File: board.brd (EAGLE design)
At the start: 92.1 x 90.5 mm, 64 parts, among them K1 FTR-K1C, K2 FTR-K1C, K3 FTR-K1C, K4 FTR-K1C, X6 PN61729-S

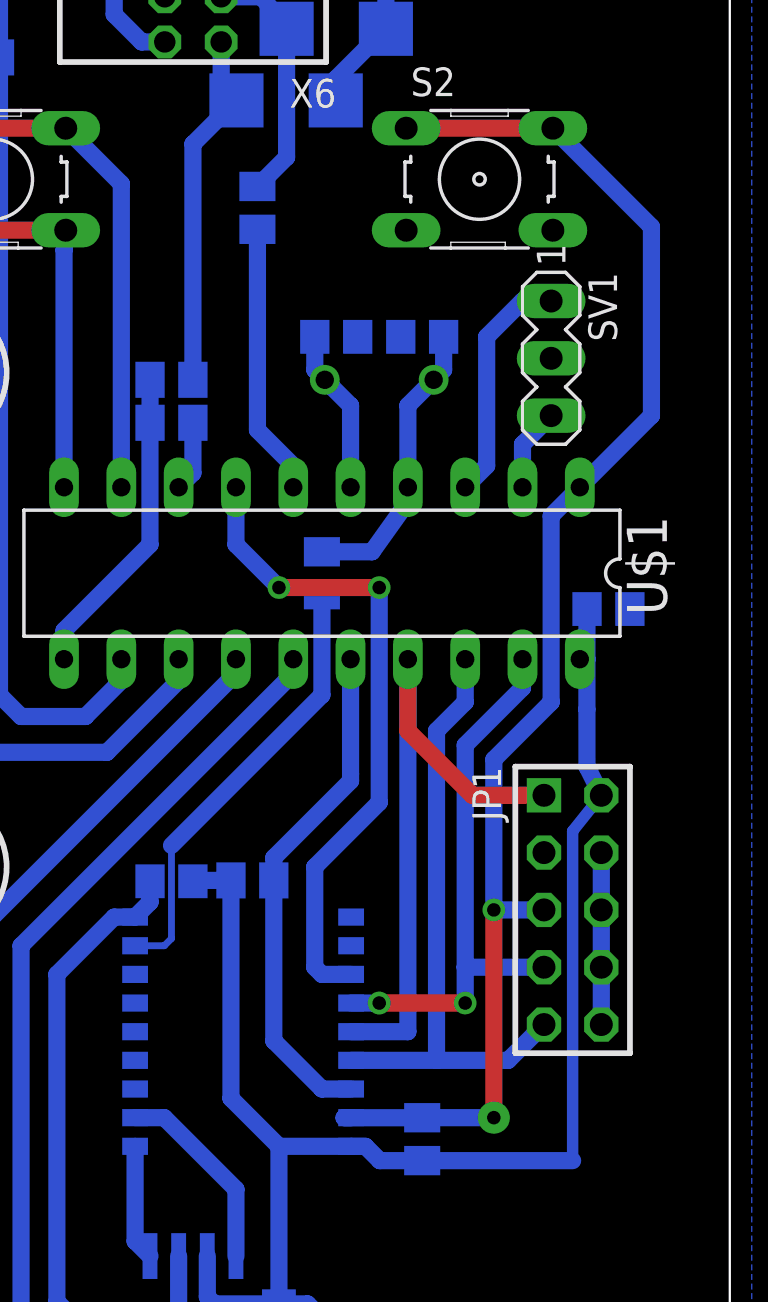
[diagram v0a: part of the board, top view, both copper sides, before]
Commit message: Moving one resistor for USB and the ISP-header
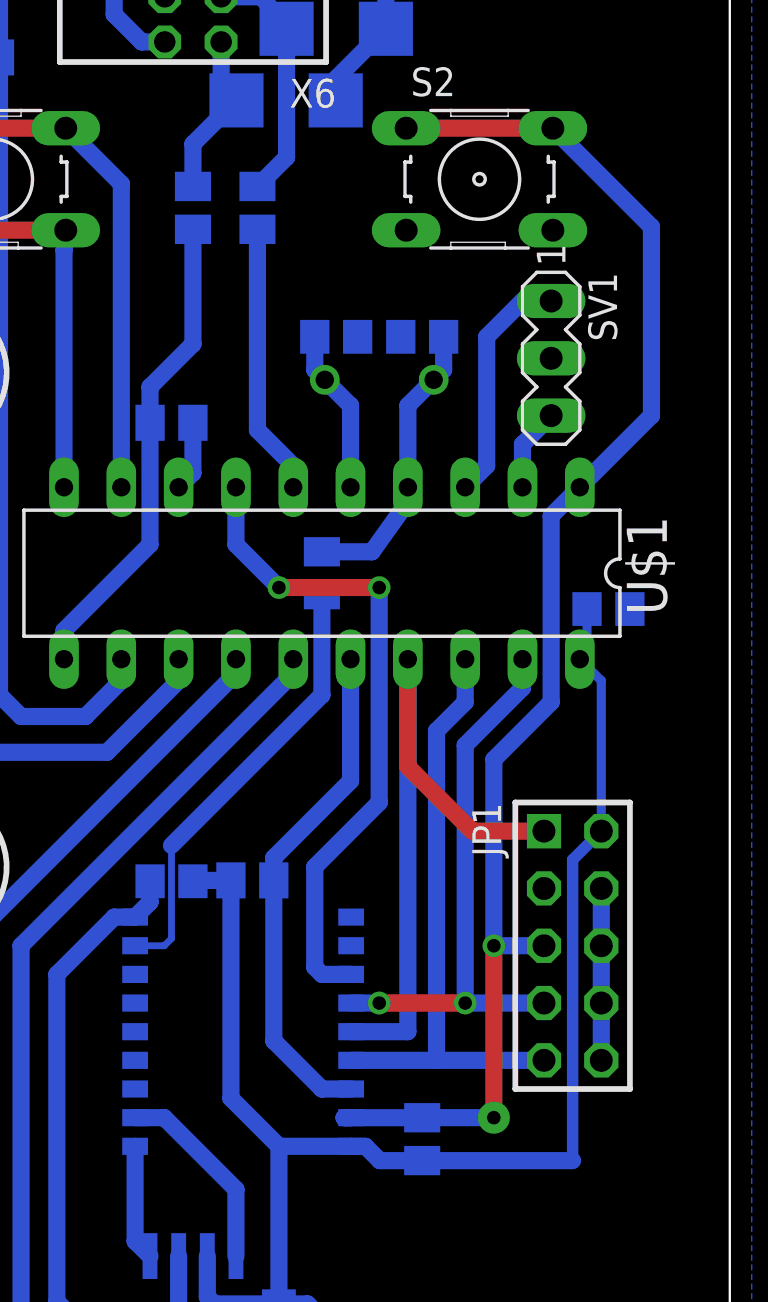
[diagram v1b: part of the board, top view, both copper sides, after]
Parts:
- moved R12 7.68 mm to (68.3, 68.3), turned to 270 degrees
- moved JP1 1.59 mm to (85.1, 35.6)
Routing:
- net N$22: track 16.1 -> 7.49 mm
- net N$24: track 14.0 -> 21.4 mm
- net MOSI: track 29.4 -> 31.0 mm
- net MISO: track 27.5 -> 26.9 mm
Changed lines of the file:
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@@
 </element>
 <element name="U$1" library="avr-7" package="DIL20" value="TINY2313-*P*" x="73.9775" y="52.07" rot="R180"/>
-<element name="JP1" library="avr-7" package="AVR-ISP-10" value="AVR-ISP-10" x="85.09" y="37.1475" rot="R270"/>
+<element name="JP1" library="avr-7" package="AVR-ISP-10" value="AVR-ISP-10" x="85.09" y="35.56" rot="R270"/>
 <element name="D1" library="diode" package="DO-214AC" value="" x="51.1175" y="19.3675" rot="MR270"/>
 <element name="D2" library="diode" package="DO-214AC" value="" x="51.1175" y="40.3225" rot="MR270"/>
@@
 </element>
 <element name="R11" library="rcl" package="M0805" value="68" x="71.12" y="68.2625" rot="MR270"/>
-<element name="R12" library="rcl" package="M0805" value="68" x="67.31" y="60.6425" rot="MR0"/>
+<element name="R12" library="rcl" package="M0805" value="68" x="68.2625" y="68.2625" rot="MR270"/>
 <element name="R13" library="rcl" package="M0805" value="1k5" x="67.31" y="58.7375" rot="MR180"/>
 <element name="D5" library="diode" package="SMB" value="3Z6" x="72.39" y="73.025" rot="MR180"/>
@@
 <contactref element="C4" pad="2"/>
 <contactref element="X6" pad="1"/>
-<wire x1="85.4075" y1="48.26" x2="85.7225" y2="48.26" width="0.762" layer="16"/>
-<wire x1="85.7225" y1="48.26" x2="85.7225" y2="46.04" width="0.762" layer="16"/>
-<wire x1="85.7225" y1="46.04" x2="85.725" y2="43.4975" width="0.762" layer="16"/>
-<wire x1="85.725" y1="43.4975" x2="86.36" y2="42.2275" width="0.762" layer="16"/>
-<wire x1="86.36" y1="42.2275" x2="85.09" y2="40.64" width="0.508" layer="16"/>
-<wire x1="85.09" y1="40.64" x2="85.09" y2="26.035" width="0.508" layer="16"/>
+<wire x1="86.36" y1="40.64" x2="85.09" y2="39.37" width="0.508" layer="16"/>
+<wire x1="85.09" y1="39.37" x2="85.09" y2="26.035" width="0.508" layer="16"/>
 <wire x1="85.09" y1="26.035" x2="78.425" y2="26.035" width="0.762" layer="16"/>
 <wire x1="78.425" y1="26.035" x2="78.4225" y2="26.0375" width="0.762" layer="16"/>
@@
 <wire x1="48.895" y1="7.9375" x2="48.895" y2="21.4125" width="0.762" layer="16"/>
 <wire x1="48.895" y1="21.4125" x2="50.6" y2="23.1175" width="0.762" layer="16"/>
-<wire x1="85.7225" y1="48.26" x2="85.7275" y2="50.4825" width="0.762" layer="16"/>
 <wire x1="50.6" y1="84.7125" x2="50.6" y2="83.1875" width="0.762" layer="16"/>
 <wire x1="50.6" y1="83.1875" x2="51.1175" y2="82.9875" width="0.762" layer="16"/>
@@
 <wire x1="73.3425" y1="6.6675" x2="74.6125" y2="7.9375" width="0.762" layer="16"/>
 <wire x1="74.6125" y1="7.9375" x2="74.6125" y2="18.415" width="0.762" layer="16"/>
+<wire x1="86.36" y1="40.64" x2="86.36" y2="47.3075" width="0.4064" layer="16"/>
+<wire x1="86.36" y1="47.3075" x2="85.4075" y2="48.26" width="0.4064" layer="16"/>
+<wire x1="85.7275" y1="50.4825" x2="85.7275" y2="48.58" width="0.4064" layer="16"/>
+<wire x1="85.7275" y1="48.58" x2="85.4075" y2="48.26" width="0.4064" layer="16"/>
 </signal>
 <signal name="N$7">
@@
 <contactref element="R16" pad="2"/>
 <contactref element="R17" pad="2"/>
-<wire x1="86.36" y1="39.6875" x2="86.36" y2="37.1475" width="0.762" layer="16"/>
-<wire x1="86.36" y1="37.1475" x2="86.36" y2="34.6075" width="0.762" layer="16"/>
-<wire x1="86.36" y1="34.6075" x2="86.36" y2="32.0675" width="0.762" layer="16"/>
+<wire x1="86.36" y1="38.1" x2="86.36" y2="35.56" width="0.762" layer="16"/>
+<wire x1="86.36" y1="35.56" x2="86.36" y2="33.02" width="0.762" layer="16"/>
+<wire x1="86.36" y1="33.02" x2="86.36" y2="30.48" width="0.762" layer="16"/>
 <via x="53.975" y="78.105" extent="1-16" drill="0.6" shape="square"/>
 <wire x1="53.975" y1="78.105" x2="53.34" y2="77.47" width="0.381" layer="1"/>
@@
 <wire x1="54.44" y1="76.8325" x2="54.44" y2="77.64" width="0.762" layer="16"/>
 <wire x1="54.44" y1="77.64" x2="53.975" y2="78.105" width="0.762" layer="16"/>
-<wire x1="86.36" y1="39.6875" x2="83.82" y2="39.6875" width="0" layer="19" extent="1-1"/>
+<wire x1="86.36" y1="38.1" x2="83.82" y2="38.1" width="0" layer="19" extent="1-1"/>
 <wire x1="53.4875" y1="35.875" x2="53.34" y2="35.56" width="0" layer="19" extent="1-16"/>
 </signal>
@@
 <wire x1="78.4225" y1="27.9375" x2="74.9579" y2="27.9375" width="0.762" layer="16"/>
 <wire x1="74.9579" y1="27.9375" x2="75.2729" y2="27.94" width="0.762" layer="16"/>
-<wire x1="83.82" y1="37.1475" x2="81.5975" y2="37.1475" width="0.762" layer="16"/>
-<via x="81.5975" y="37.1475" extent="1-16" drill="0.6" diameter="0.8128" shape="octagon"/>
-<wire x1="81.5975" y1="37.1475" x2="81.5975" y2="27.94" width="0.762" layer="1"/>
+<wire x1="83.82" y1="35.56" x2="81.5975" y2="35.56" width="0.762" layer="16"/>
+<via x="81.5975" y="35.56" extent="1-16" drill="0.6" diameter="0.8128" shape="octagon"/>
+<wire x1="81.5975" y1="35.56" x2="81.5975" y2="27.94" width="0.762" layer="1"/>
 <via x="81.5975" y="27.94" extent="1-16" drill="0.6" diameter="1.4224" shape="octagon"/>
 <wire x1="81.5975" y1="27.94" x2="78.425" y2="27.94" width="0.762" layer="16"/>
@@
 <wire x1="84.1375" y1="54.61" x2="84.1375" y2="46.355" width="0.762" layer="16"/>
 <wire x1="84.1375" y1="46.355" x2="81.5975" y2="43.815" width="0.762" layer="16"/>
-<wire x1="81.5975" y1="43.815" x2="81.5975" y2="37.1475" width="0.762" layer="16"/>
+<wire x1="81.5975" y1="43.815" x2="81.5975" y2="35.56" width="0.762" layer="16"/>
 <wire x1="84.1375" y1="54.61" x2="85.4075" y2="55.88" width="0.762" layer="16"/>
 <wire x1="84.2137" y1="71.7931" x2="88.5825" y2="67.4243" width="0.762" layer="16"/>
@@
 <wire x1="82.8675" y1="48.26" x2="82.8675" y2="46.99" width="0.762" layer="16"/>
 <wire x1="82.8675" y1="46.99" x2="80.3275" y2="44.45" width="0.762" layer="16"/>
-<wire x1="80.3275" y1="34.6075" x2="83.82" y2="34.6075" width="0.762" layer="16"/>
+<wire x1="80.3275" y1="33.02" x2="83.82" y2="33.02" width="0.762" layer="16"/>
 <wire x1="75.2729" y1="33.02" x2="76.5175" y2="33.02" width="0.762" layer="16"/>
 <via x="76.5175" y="33.02" extent="1-16" drill="0.6" diameter="1.016" shape="octagon"/>
 <wire x1="76.5175" y1="33.02" x2="80.3275" y2="33.02" width="0.762" layer="1"/>
 <via x="80.3275" y="33.02" extent="1-16" drill="0.6" shape="octagon"/>
-<wire x1="80.3275" y1="44.45" x2="80.3275" y2="34.6075" width="0.762" layer="16"/>
-<wire x1="80.3275" y1="34.6075" x2="80.3275" y2="33.02" width="0.762" layer="16"/>
+<wire x1="80.3275" y1="44.45" x2="80.3275" y2="33.02" width="0.762" layer="16"/>
 </signal>
 <signal name="MISO">
@@
 <wire x1="79.0575" y1="45.085" x2="80.3275" y2="46.355" width="0.762" layer="16"/>
 <wire x1="80.3275" y1="46.355" x2="80.3275" y2="48.26" width="0.762" layer="16"/>
-<wire x1="79.0575" y1="30.48" x2="82.2325" y2="30.48" width="0.762" layer="16"/>
-<wire x1="82.2325" y1="30.48" x2="83.82" y2="32.0675" width="0.762" layer="16"/>
+<wire x1="79.0575" y1="30.48" x2="83.82" y2="30.48" width="0.762" layer="16"/>
 </signal>
 <signal name="MOSI">
@@
 <wire x1="75.2729" y1="31.75" x2="77.7875" y2="31.75" width="0.762" layer="16"/>
 <wire x1="77.7875" y1="48.26" x2="77.7875" y2="31.75" width="0.762" layer="16"/>
-<wire x1="83.82" y1="42.2275" x2="80.645" y2="42.2275" width="0.762" layer="1"/>
-<wire x1="80.645" y1="42.2275" x2="77.7875" y2="45.085" width="0.762" layer="1"/>
-<wire x1="77.7875" y1="45.085" x2="77.7875" y2="48.26" width="0.762" layer="1"/>
+<wire x1="83.82" y1="40.64" x2="80.645" y2="40.64" width="0.762" layer="1"/>
+<wire x1="80.645" y1="40.64" x2="77.7875" y2="43.4975" width="0.762" layer="1"/>
+<wire x1="77.7875" y1="43.4975" x2="77.7875" y2="48.26" width="0.762" layer="1"/>
 </signal>
 <signal name="CS">
@@
 <wire x1="69.5125" y1="73.7025" x2="70.19" y2="73.025" width="0.762" layer="16"/>
 <wire x1="70.19" y1="73.025" x2="68.26" y2="71.095" width="0.762" layer="16"/>
-<wire x1="68.26" y1="71.095" x2="68.26" y2="60.6425" width="0.762" layer="16"/>
+<wire x1="68.26" y1="71.095" x2="68.2625" y2="69.2125" width="0.762" layer="16"/>
 </signal>
 <signal name="N$24">
@@
 <wire x1="66.3575" y1="53.34" x2="66.3575" y2="58.735" width="0.762" layer="16"/>
 <wire x1="66.3575" y1="58.735" x2="66.36" y2="58.7375" width="0.762" layer="16"/>
-<wire x1="66.36" y1="58.7375" x2="66.36" y2="60.6425" width="0.762" layer="16"/>
+<wire x1="68.2625" y1="67.3125" x2="68.2625" y2="62.23" width="0.762" layer="16"/>
+<wire x1="68.2625" y1="62.23" x2="66.3575" y2="60.325" width="0.762" layer="16"/>
+<wire x1="66.3575" y1="60.325" x2="66.3575" y2="58.74" width="0.762" layer="16"/>
+<wire x1="66.3575" y1="58.74" x2="66.36" y2="58.7375" width="0.762" layer="16"/>
 </signal>
 <signal name="N$25">

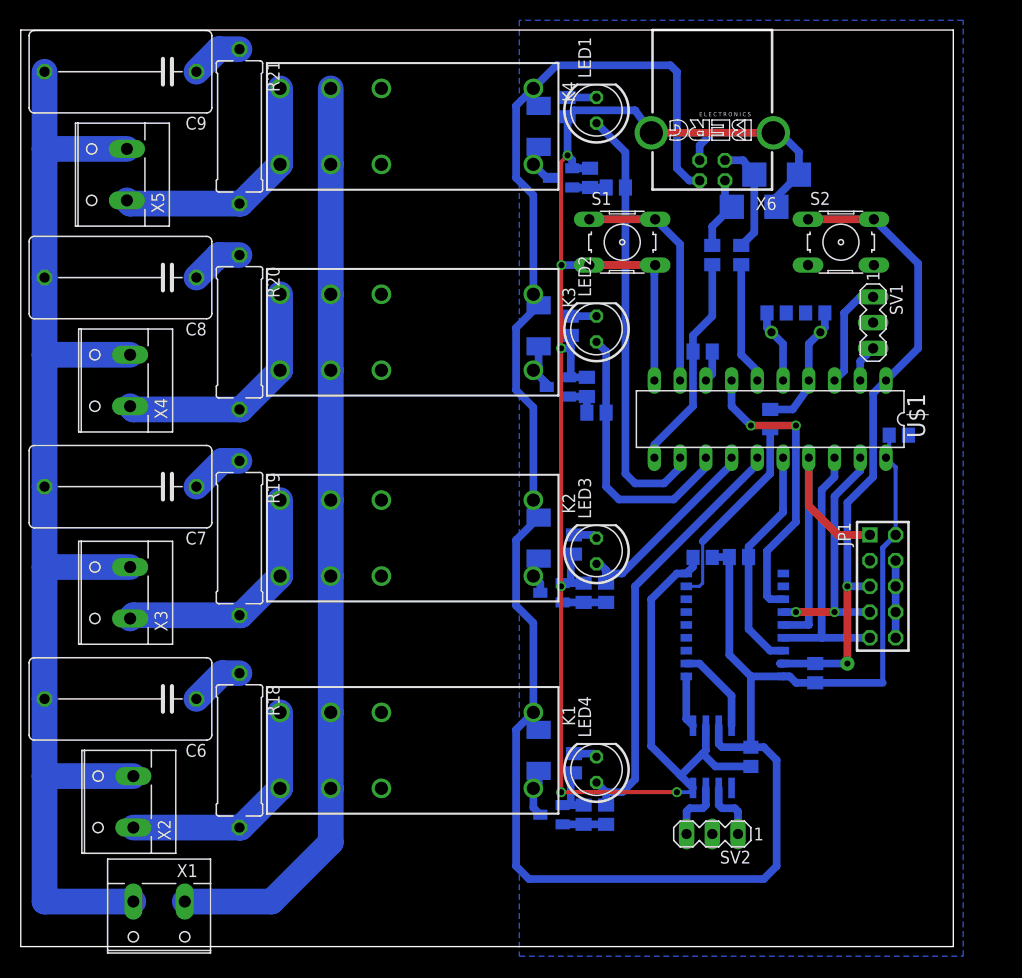
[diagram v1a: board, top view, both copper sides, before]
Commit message: Adding choice of powersupply, enhancing supply of the tiny, board is a touch larger
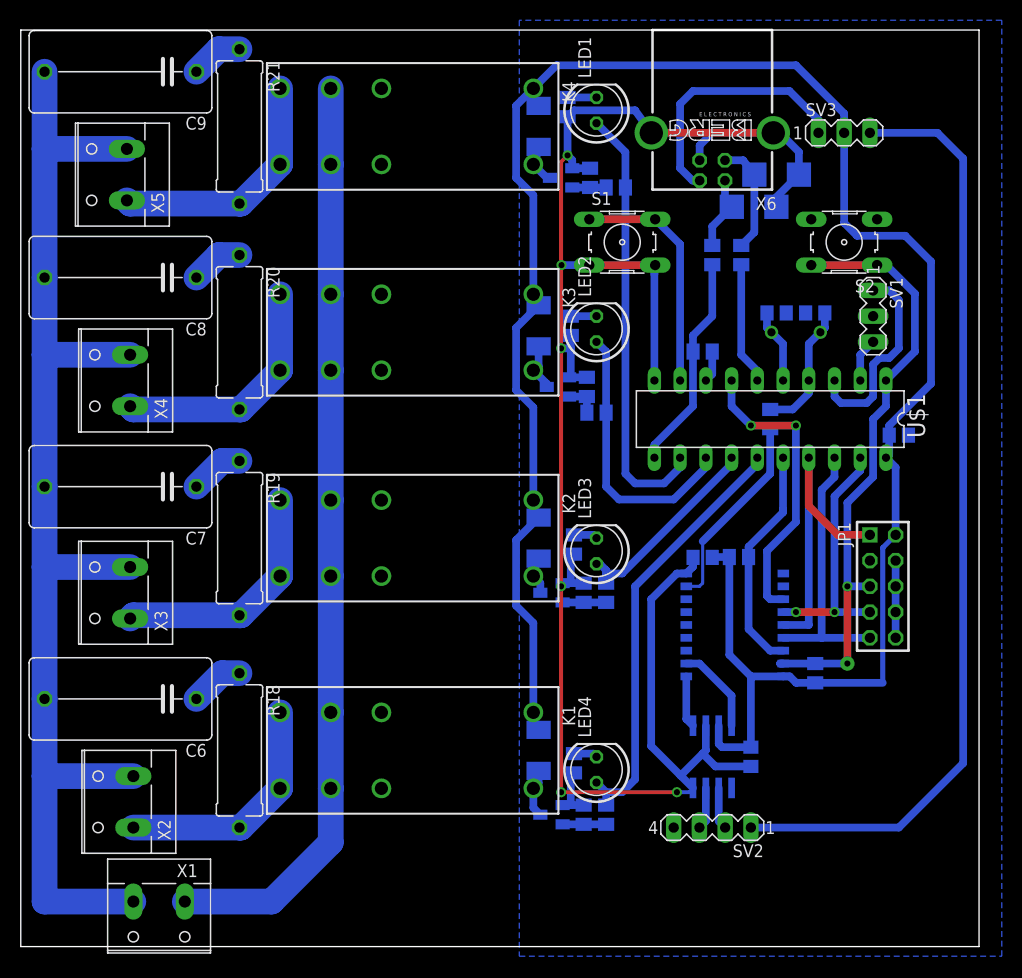
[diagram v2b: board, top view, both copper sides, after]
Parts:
- added SV3: (no value), con-lstb:MA03-1
- SV2: device con-lstb:MA03-1 -> con-lstb:MA04-1
- moved SV2 0.63 mm to (68.3, 11.7)
- moved SV1 0.63 mm to (84.1, 62.2)
- moved S2 0.32 mm to (81.3, 69.5), turned to 180 degrees
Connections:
- new net +5V/1: SV3.1, X6.1
- new net +5V/2: SV2.1, SV3.3
- net +5V: now also SV3.2; no longer X6.1
- net GND: now also SV2.4; no longer SV2.2
- net N$35: now also SV2.2; no longer SV2.1
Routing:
- net +5V/2: track 0.00 -> 93.5 mm
- net +5V/1: track 0.00 -> 25.4 mm
- net +5V: track 221.4 -> 211.0 mm
- net N$25: track 10.6 -> 20.0 mm
- net RESET: track 64.2 -> 59.9 mm
- net N$34: track 6.08 -> 4.17 mm
- net N$35: track 6.08 -> 4.17 mm
- net N$26: track 3.70 -> 4.34 mm
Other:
- board size 92.1 x 90.5 mm -> 94.6 x 90.5 mm
